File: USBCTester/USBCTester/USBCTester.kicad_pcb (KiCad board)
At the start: 4 copper layers, 100 x 82.6 mm, 95 parts, among them J1 USB4080-03-A, J2 USB4080-03-A, J3 Conn_01x14, J4 Conn_01x03, J6 Conn_01x03, SW1 SW_Push, U1 74HC595, U2 74HC595, U3 74HC595, U4 74HC595, U5 74HC595, U6 74HC595, U7 RaspberryPi_Pico

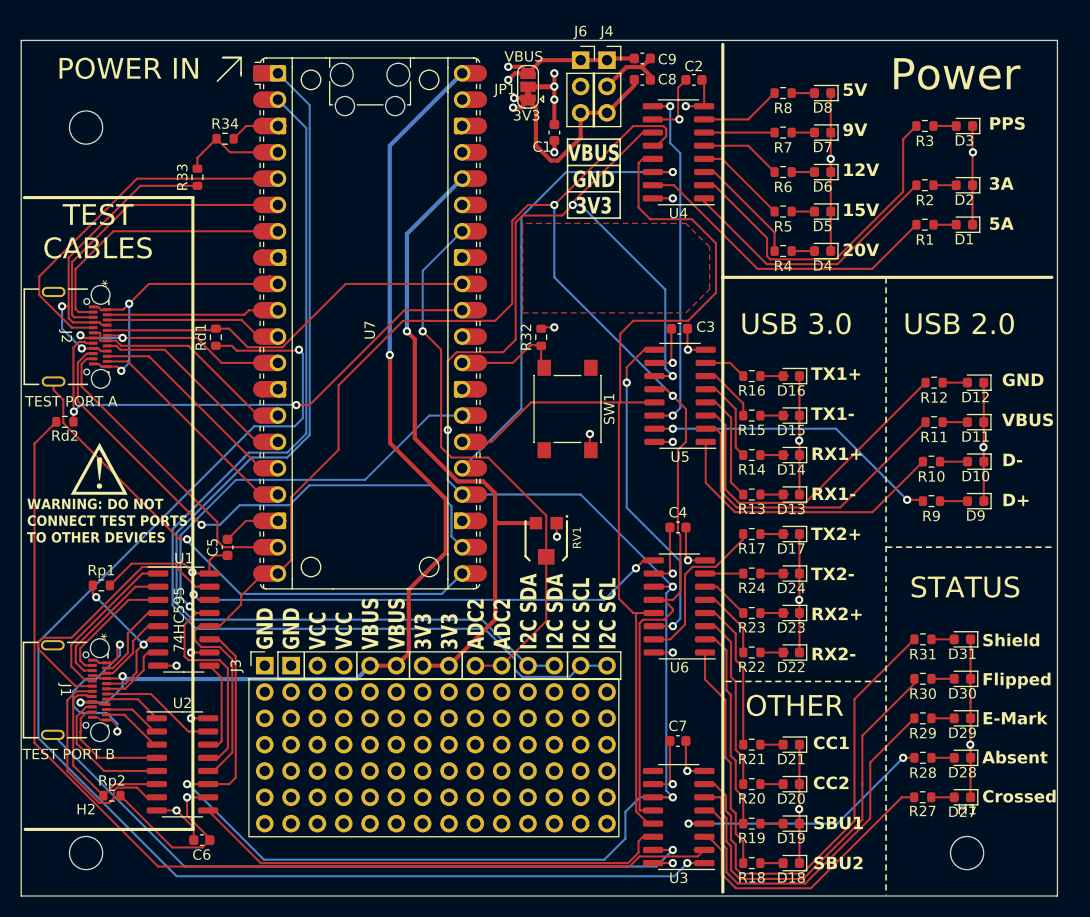
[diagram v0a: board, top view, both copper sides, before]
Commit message: use older footprint for USBC since JLCPCB does seem to tolerate the shape, and minor silkscreen fixes
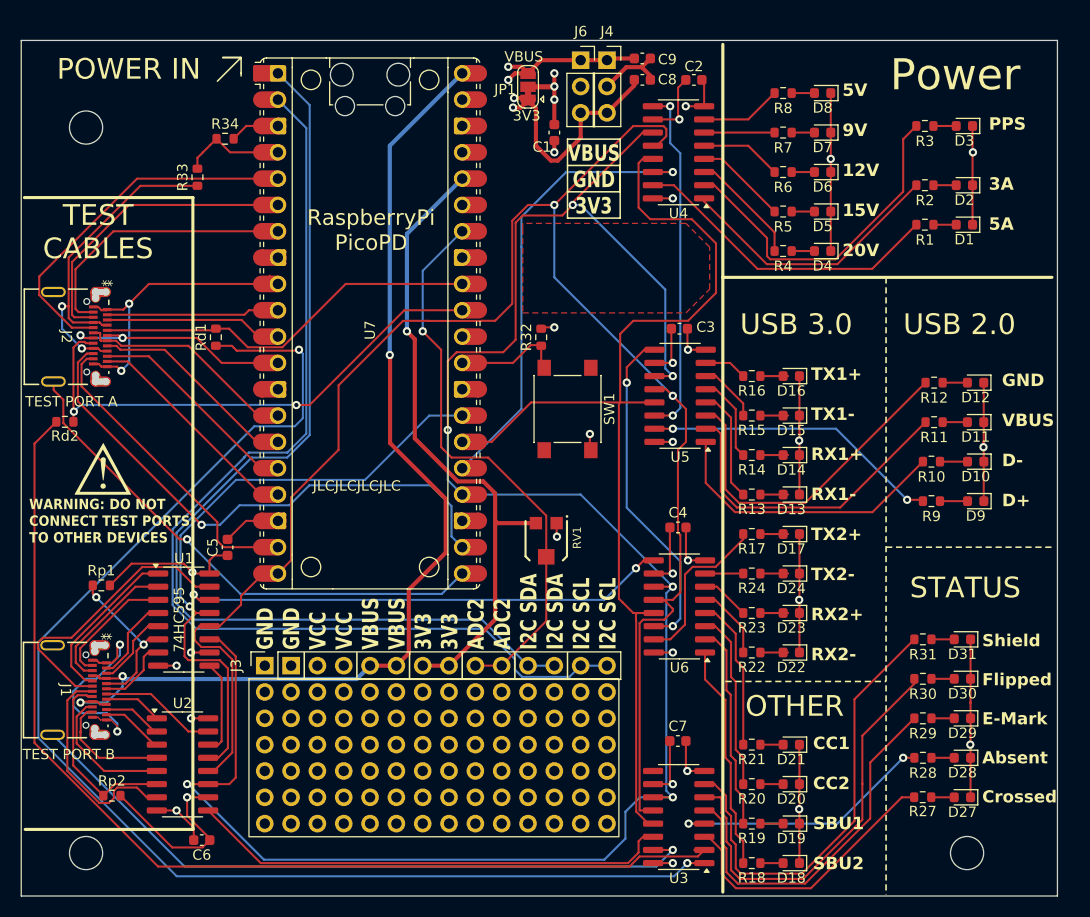
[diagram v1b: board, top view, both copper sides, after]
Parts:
- J1, J2: footprint USBCFootprint:USB4080-03-A_GCT_RoundHoles -> USBCFootprint:USB4080-03-A_GCT_PlatedHoles
- U7: value RaspberryPi_Pico -> RaspberryPi PicoPD
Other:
- board text added: "JLCJLCJLCJLC"
- board text added: "RaspberryPi PicoPD"
